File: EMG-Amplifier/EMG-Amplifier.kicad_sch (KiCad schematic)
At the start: 29 parts, among them U1 LM324, U2 LM741, U3 LM741, U4 LM741, U9 LM324

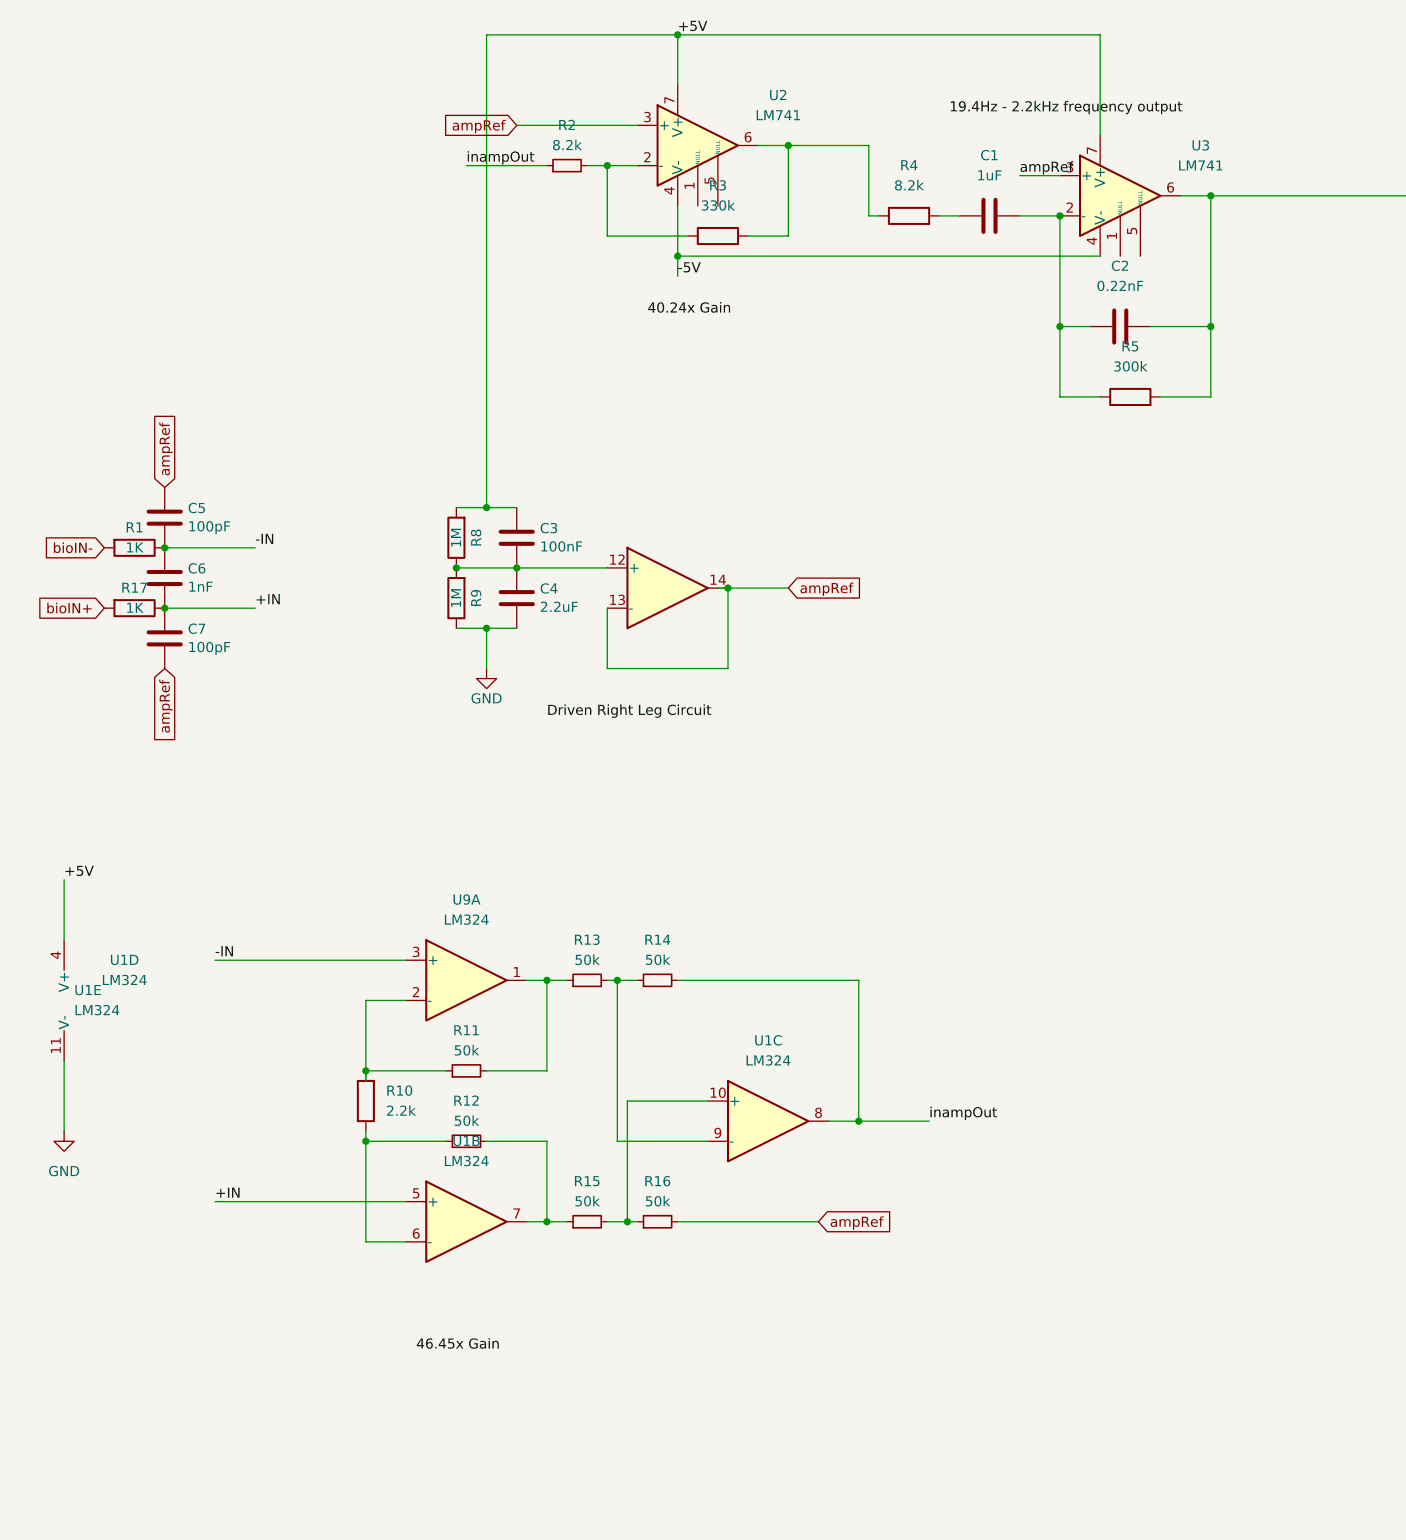
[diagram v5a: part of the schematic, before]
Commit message: Code for adc fft and windowing added
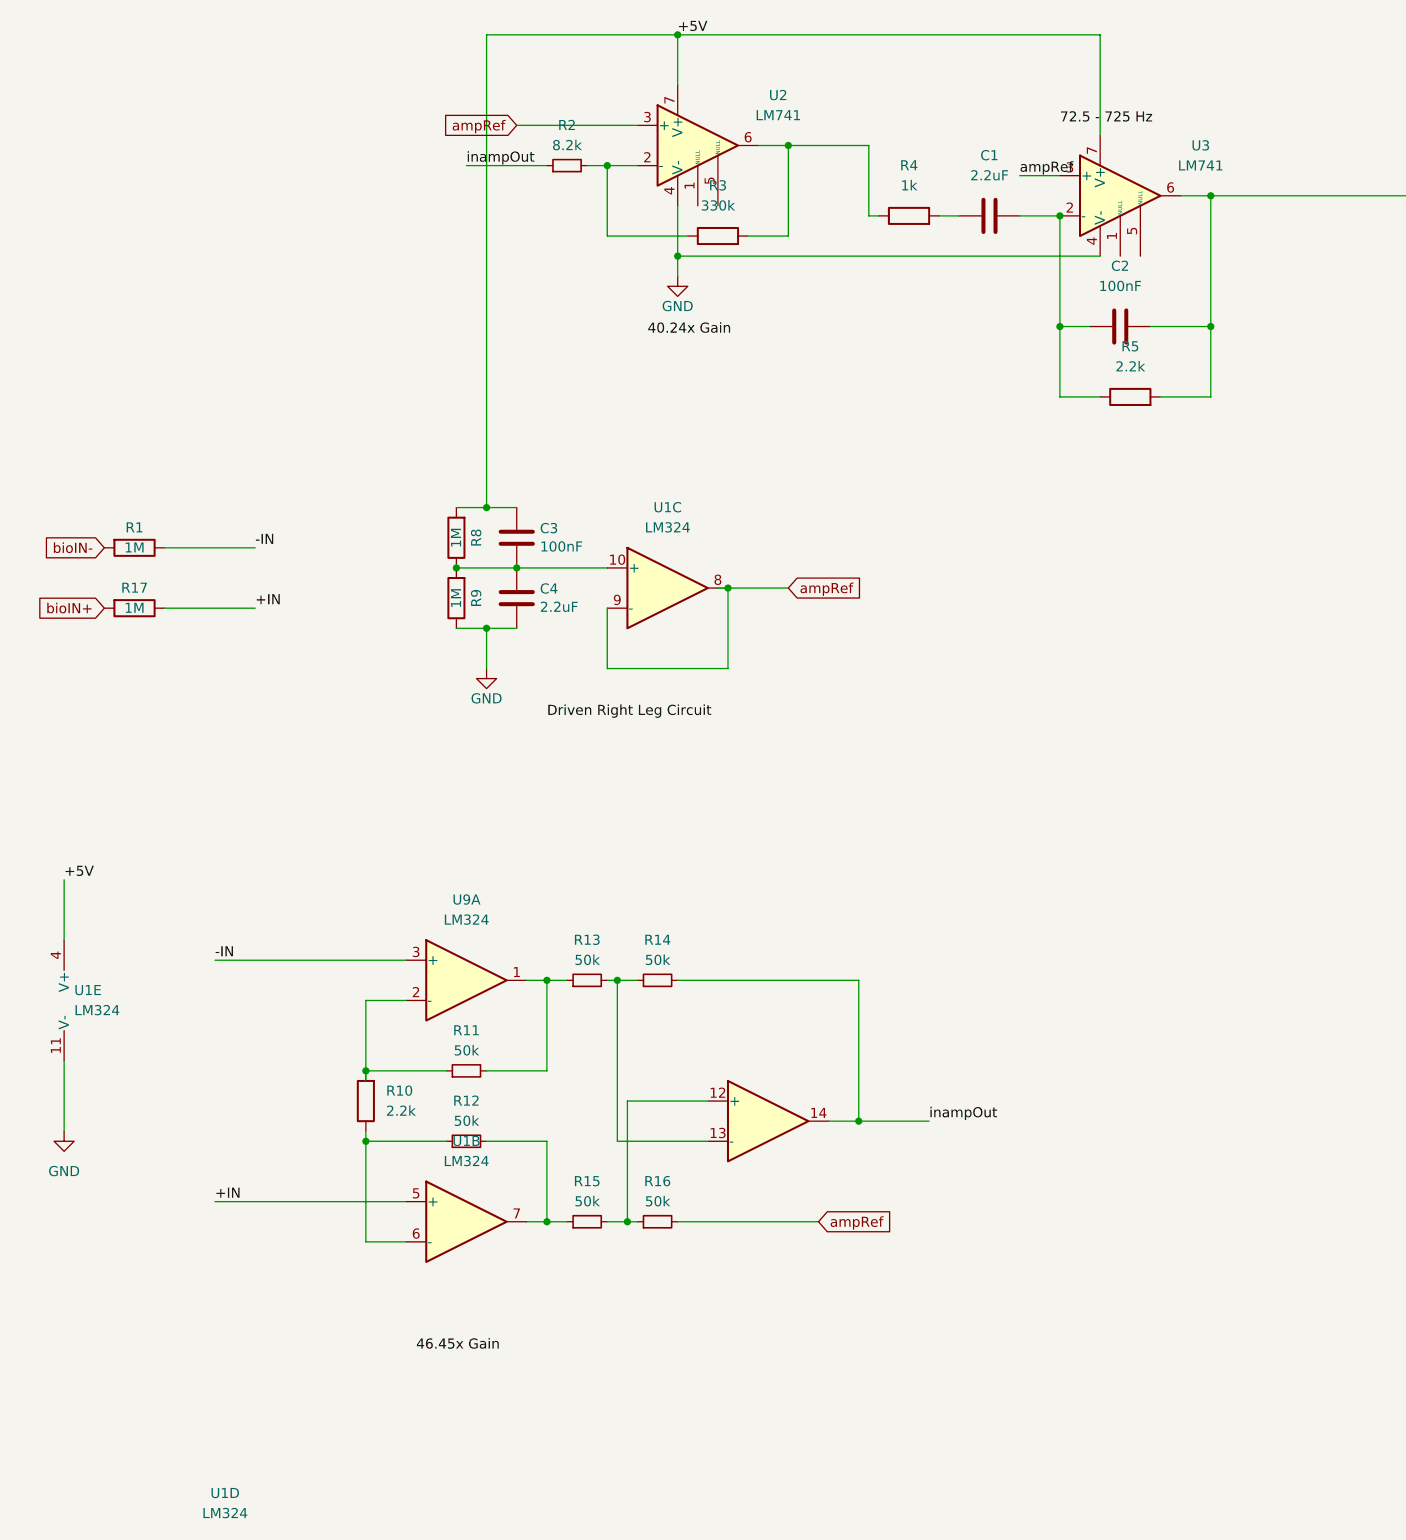
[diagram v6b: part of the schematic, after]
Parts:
- removed C5, C7: 100pF, Capacitor_SMD:C_0805_2012Metric_Pad1.18x1.45mm_HandSolder, symbol Device:C
- removed C6: 1nF, Capacitor_SMD:C_0805_2012Metric_Pad1.18x1.45mm_HandSolder, symbol Device:C
- C1: value 1uF -> 2.2uF
- C2: value 0.22nF -> 100nF
- R1, R17: value 1K -> 1M
- R4: value 8.2k -> 1k
- R5: value 300k -> 2.2k
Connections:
- net -5V is gone; now on net GND: U2.4 (V-), U3.4 (V-)
- net ampRef: now also U1.8, U1.9 (-); no longer U1.13 (-), U1.14
- net inampOut: now also U1.14; no longer U1.8
- net at C3.1, C4.2, R8.1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: now also U1.10 (+); no longer U1.12 (+)
- net at R15.2, R16.1: now also U1.12 (+); no longer U1.10 (+)
- net at R13.2, R14.1: now also U1.13 (-); no longer U1.9 (-)
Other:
- moved on the sheet: U1C, U1D

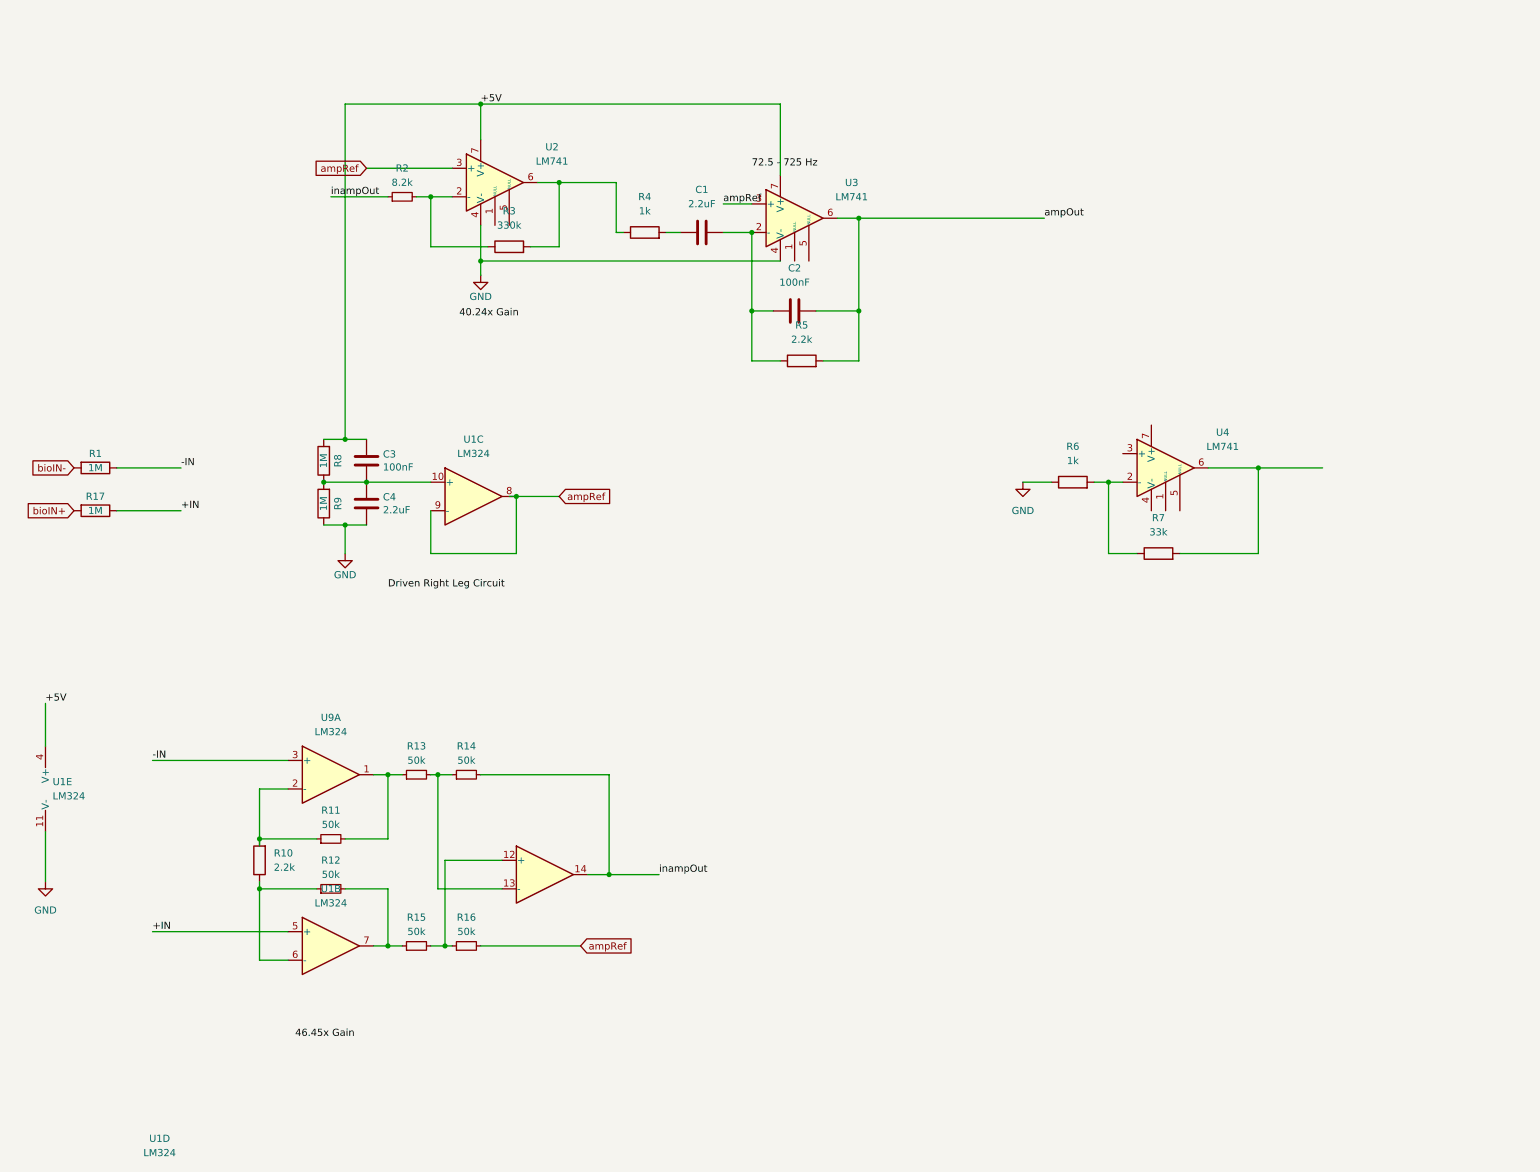
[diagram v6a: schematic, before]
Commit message: Add the datafiles  (#6)
* Removed the Emg-firmware
* Updated the code for 3 patchy sensors
* Added the HTTP Server code
* Added the single channel and wifi handler
* Added code for better signal reading and the data processing code
* Added data files and removed the unwanted ones
* Structured the Files
* Undo changes to model_cnn_lstm.py
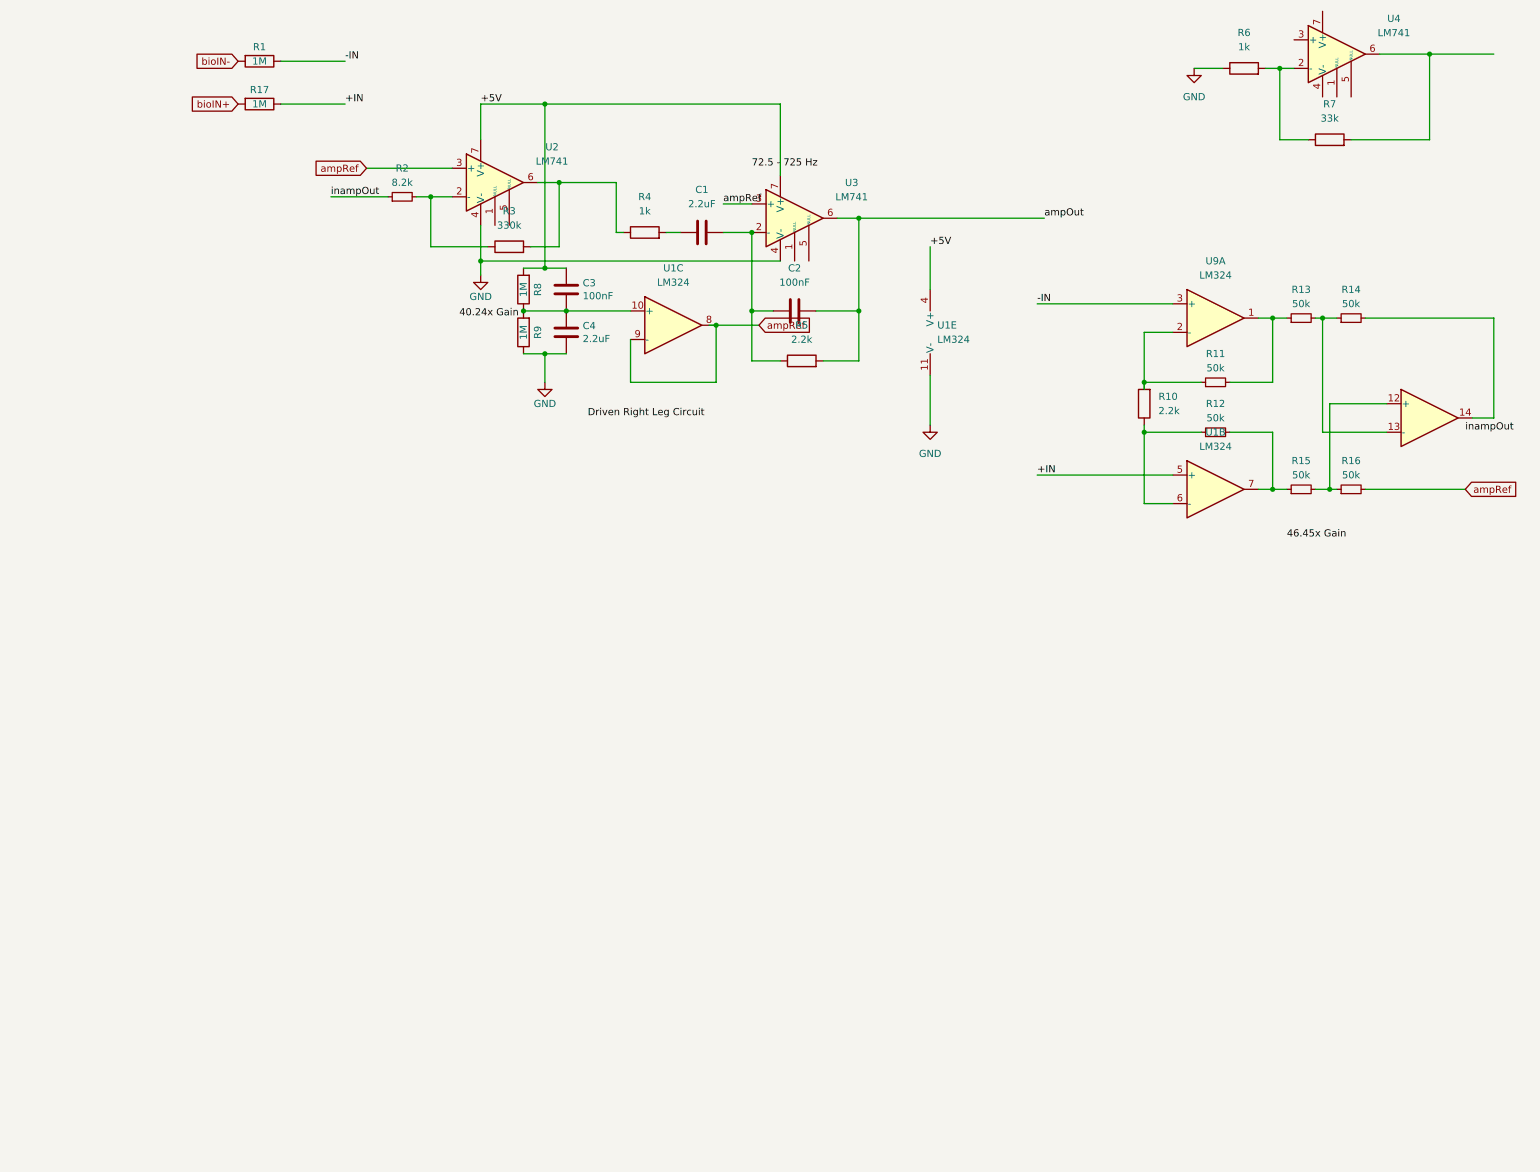
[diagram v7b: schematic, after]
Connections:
- net inampOut: no longer R14.2, U1.14
- new net: R14.2, U1.14
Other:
- moved on the sheet: C3, C4, R1, R10, R11, R12, R13, R14, R15, R16, R17, R6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
